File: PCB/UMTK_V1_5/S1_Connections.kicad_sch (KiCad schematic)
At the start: 15 parts

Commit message: Put in Files for V1
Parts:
- removed J?: JST 4pin, 4Pin JST, symbol UMTK-altium-import:2_4Pin JST
- removed J?: JST 4pin, 4Pin JST, symbol UMTK-altium-import:0_4Pin JST
- removed P?: SCREW-5.0/5.08 2WAYS, SCREW-5.0-2WAYS_V, symbol UMTK-altium-import:2_SCREW-2WAYS
- removed P? (x2): SCREW-5.0/5.08 2WAYS, SCREW-5.0-2WAYS_V, symbol UMTK-altium-import:0_SCREW-2WAYS
- removed U?: L7805_Side, TO220_Side Mount, symbol UMTK-altium-import:0_L7805_Side
- removed X?: HX711_Board, HX711_Board_Large, symbol UMTK-altium-import:0_HX711_Board
- added C? (x2): 1000u, Alu Cap 6.3x2.5mm, symbol UMTK-altium-import:0_Polar Cap
- added C?: 220u, Alu Cap 6.3x2.5mm, symbol UMTK-altium-import:0_Polar Cap
- added D?: MBR0560, Diode_SMD:D_SOD-123, symbol Diode:MBR0560
- added J?: Power IN, symbol Connector:Screw_Terminal_01x02
- added JP?: Slide_CLK_Swap, symbol Jumper:Jumper_3_Bridged12
- added JP?: Slide_DAT_Swap, symbol Jumper:Jumper_3_Bridged12
- added JP?: SlidePower, symbol Jumper:Jumper_3_Bridged12
- added L?: 100u, symbol Device:L
- added U?: LM2576HVS-5, Package_TO_SOT_SMD:TO-263-5_TabPin3, symbol Regulator_Switching:LM2576HVS-5
- C?: value 220u -> 100u 24v
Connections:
- net +3V3: now also C?.1, JP?.1 (A); no longer J?.1, J?.1 (VBUS), J?.1 (VBUS)
- net GND: now also C?.2, C?.2, C?.2, D?.2 (A), J?.2 (Pin_2), U?.3 (GND), U?.5 (~{ON}/OFF)
- net SLIDE_CLK: now also JP?.1 (A), JP?.2 (C), JP?.3 (B)
- net SLIDE_DAT: now also JP?.1 (A), JP?.2 (C), JP?.3 (B)
- net +5 renamed +5V
- net +5V: now also C?.1, C?.1, JP?.3 (B), L?.2, U?.4 (FB)
- net Vin renamed +12V
- net +12V: now also J?.1 (Pin_1), U?.1 (VIN)
- new net: J?.1, J?.1 (VBUS), J?.1 (VBUS), JP?.2 (C)
- new net: D?.1 (K), L?.1, U?.2 (OUT)
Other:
- note removed: "Loadcell Connections"
- note removed: "Motor Connections"
- moved on the sheet: C?, J?

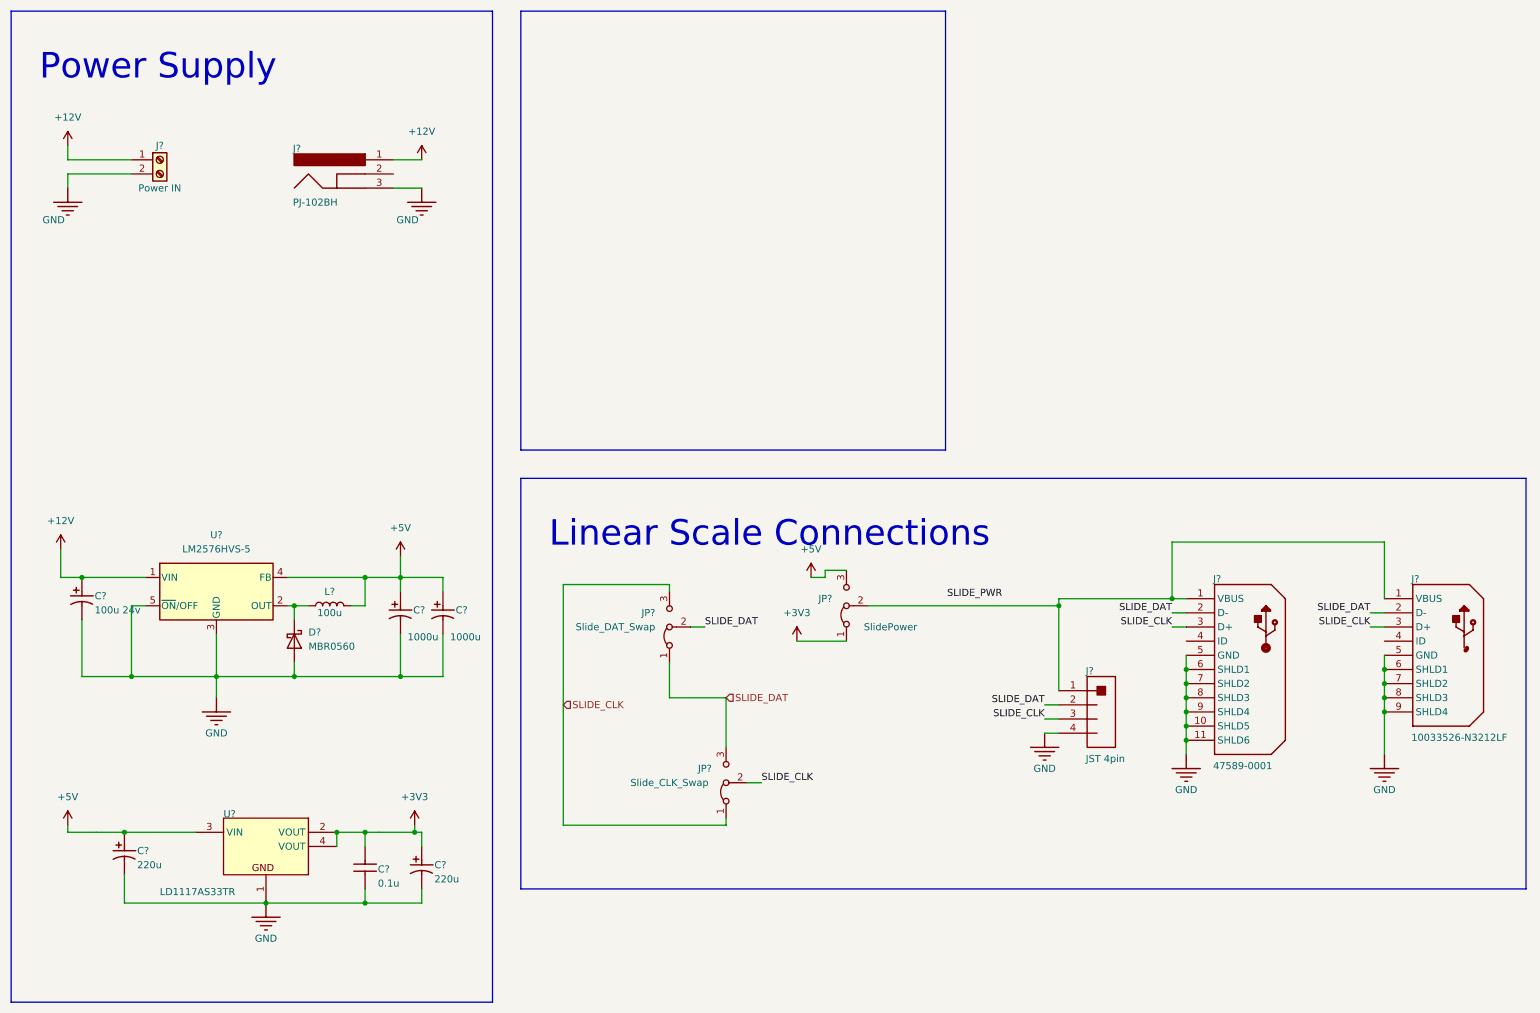
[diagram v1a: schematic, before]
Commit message: Updated Schematics
Done: 7 Seg, Power, Motor, Slide, HX711
To Do: Arduino
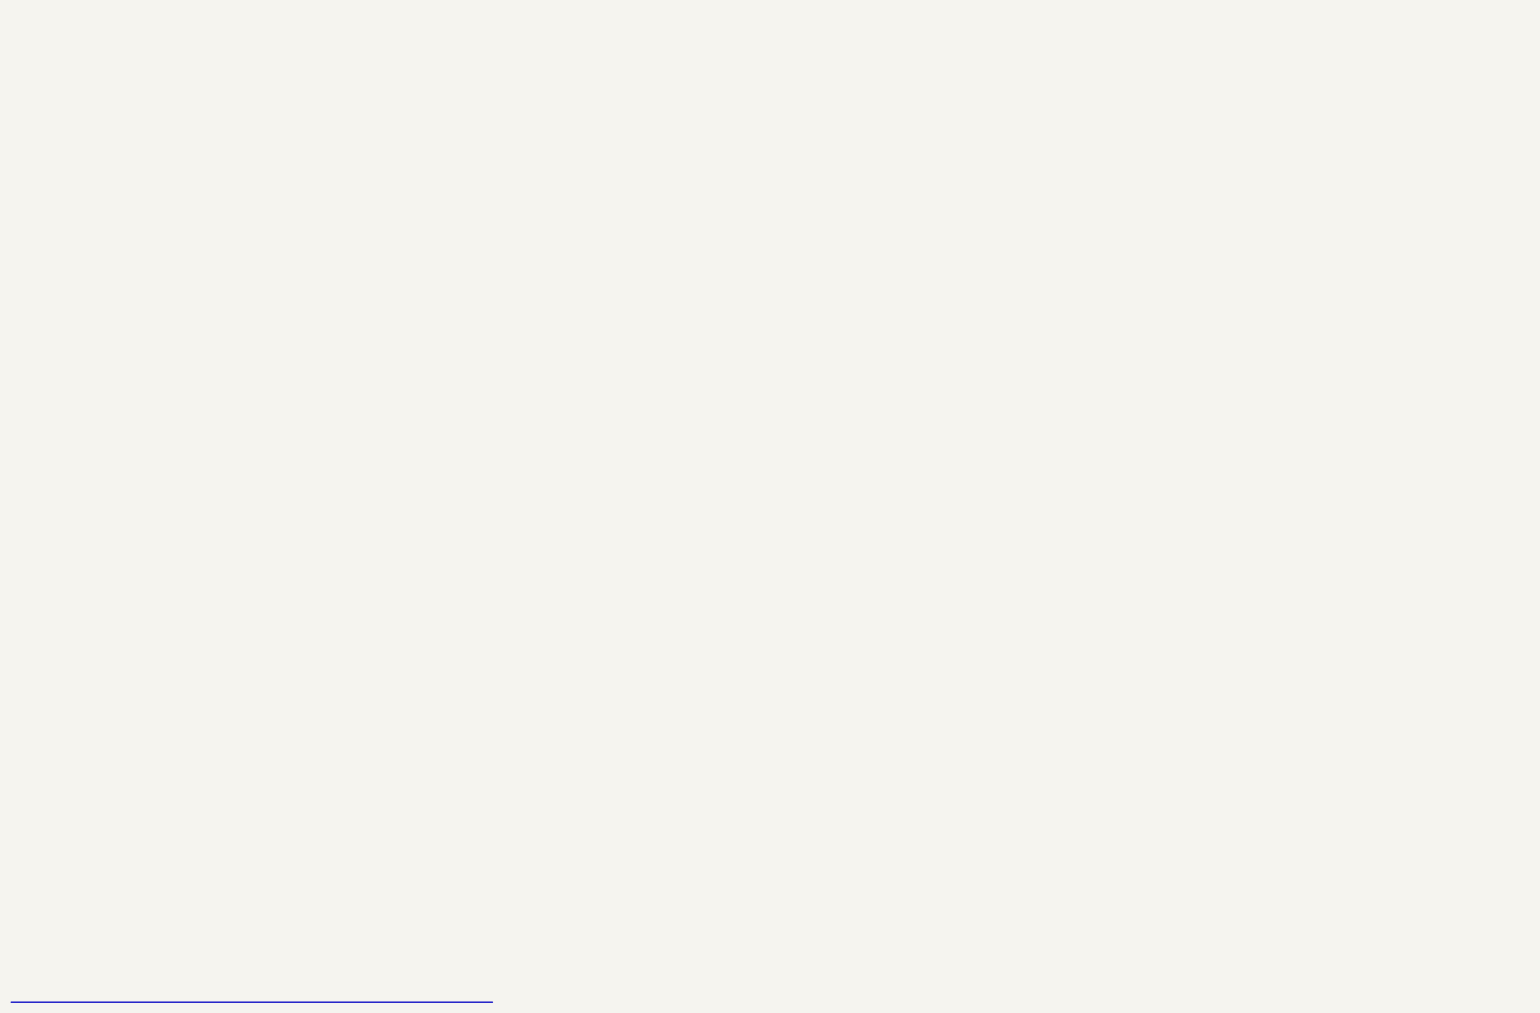
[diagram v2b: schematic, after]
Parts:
- removed C? (x2): 1000u, Alu Cap 6.3x2.5mm, symbol UMTK-altium-import:0_Polar Cap
- removed C? (x2): 220u, Alu Cap 6.3x2.5mm, symbol UMTK-altium-import:0_Polar Cap
- removed C?: 0.1u, Ceramic Cap 5mm, symbol UMTK-altium-import:0_Cap
- removed C?: 100u 24v, Alu Cap 6.3x2.5mm, symbol UMTK-altium-import:0_Polar Cap
- removed D?: MBR0560, Diode_SMD:D_SOD-123, symbol Diode:MBR0560
- removed J?: 47589-0001, MOLX-47589-0001_V, symbol UMTK-altium-import:0_USB-5-6SHLD
- removed J?: PJ-102BH, CUI-PJ-102BH_V, symbol UMTK-altium-import:0_JACK-2CD3-RN
- removed J?: Power IN, symbol Connector:Screw_Terminal_01x02
- removed J?: 10033526-N3212LF, FCI-10033526-N3212LF_V, symbol UMTK-altium-import:0_USB-5-4SHLD
- removed J?: JST 4pin, 4Pin JST, symbol UMTK-altium-import:0_4Pin JST
- removed JP?: Slide_CLK_Swap, symbol Jumper:Jumper_3_Bridged12
- removed JP?: Slide_DAT_Swap, symbol Jumper:Jumper_3_Bridged12
- removed JP?: SlidePower, symbol Jumper:Jumper_3_Bridged12
- removed L?: 100u, symbol Device:L
- removed U?: LM2576HVS-5, Package_TO_SOT_SMD:TO-263-5_TabPin3, symbol Regulator_Switching:LM2576HVS-5
- removed U?: LD1117AS33TR, SOT-223_M, symbol UMTK-altium-import:0_PM-REG-LD1117-SOT4
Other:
- note removed: "Linear Scale Connections"
- note removed: "Power Supply"
